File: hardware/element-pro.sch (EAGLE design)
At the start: 80 parts, among them J4 AMP FCI 10103594-0001LF, Q3 BSS138PW,115, Q4 BSS138PW,115, SW1 SPST_TACT-KMR2, U1 NEOPIXEL_NANO_2427, U10 TSL2591, U11 915MHz, U12 W25X40CLSNIG-ND-AT25F512BJEDE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, U14 SENSEAIR_S8, U15 VLP-450-F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

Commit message: v0.2 - design update
- moved T/RH sensor away from top
- moved thermistor + ADC away from top
- moved VOC sensor from bottom
- repositioned pressure sensor
- added more isolation to all necessary sensors
- a lot of trace and component placement adjustments
- added external voltage input
- ERC/DRC
- silkscreen update
- added gerbers
- NOTE: BOM not updated; untested design
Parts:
- added C14: 0.1uF, Adafruit Feather 32u4 Bluefruit LE:MICROBUILDER_CAP_CERAMIC_0402MP
- added J3: (no value), SparkFun-Connectors:CONN_022.54MM_SCREWTERM
- added R1, R2: 10K, Adafruit Feather 32u4 Bluefruit LE:MICROBUILDER_RESISTOR_0402MP
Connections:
- removed net AIN1: U4.AIN1
- new net AIN3: R1.2, U4.AIN3
- new net N$6: C14.2, J3.2, R1.1, R2.2
- net GND: now also C14.1, J3.1, R2.1
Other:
- note added: "0.2"
- note added: "External voltage input"
- note removed: "0.1"
- moved on the sheet: C13, C2, FB3, FB4, R12, U4

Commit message: branding modification
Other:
- note added: "0.3"
- note removed: "0.2"
- note removed: "ArchSense"
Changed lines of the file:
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@@
 <?xml version="1.0" encoding="utf-8"?>
 <!DOCTYPE eagle SYSTEM "eagle.dtd">
-<eagle version="9.4.1">
+<eagle version="9.1.1">
 <drawing>
 <settings>
@@
 <text x="-60.96" y="129.54" size="2.54" layer="94" font="vector">TagConnect ISP headers</text>
 <text x="241.3" y="-25.4" size="2.54" layer="94" font="vector">3.3V voltage regulator</text>
-<text x="248.412" y="-82.296" size="5.08" layer="94" font="vector" ratio="20">ArchSense</text>
-<text x="248.666" y="-74.422" size="2.54" layer="94" font="vector" ratio="10">Element Pro</text>
+<text x="245.872" y="-79.756" size="5.08" layer="94" font="vector" ratio="20">Element Pro</text>
 <text x="257.302" y="-112.522" size="2.54" layer="94" font="vector" ratio="10">Akram Ali</text>
 <text x="134.62" y="-30.48" size="2.54" layer="94" font="vector">USB + FTDI</text>
-<text x="257.556" y="-102.362" size="2.54" layer="94" font="vector" ratio="10">0.2</text>
-<text x="248.666" y="-87.122" size="2.54" layer="94" font="vector" ratio="10">github.com/akstudios</text>
+<text x="257.556" y="-102.362" size="2.54" layer="94" font="vector" ratio="10">0.3</text>
+<text x="246.126" y="-84.582" size="2.54" layer="94" font="vector" ratio="10">github.com/akstudios</text>
 <text x="160.02" y="101.6" size="1.778" layer="97" font="vector">0x29</text>
 <text x="208.28" y="76.2" size="2.54" layer="94" font="vector">RGB LED</text>

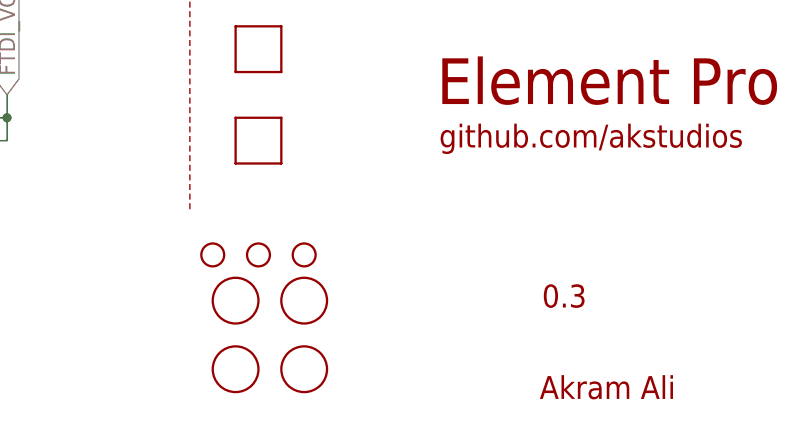
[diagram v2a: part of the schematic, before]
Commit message: v0.4 - repositioning sensors
- better heat management
- added more thermal breaks on board
- rearranged many traces
- erc/drc
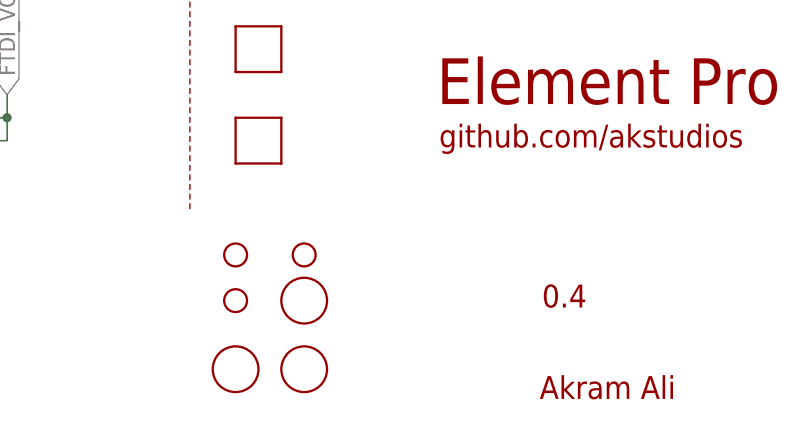
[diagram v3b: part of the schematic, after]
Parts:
- removed U$7: FIDUCIAL, adafruit:FIDUCIAL
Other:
- note added: "0.4"
- note removed: "0.3"
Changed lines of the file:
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@@
 <part name="SUPPLY21" library="SparkFun-Aesthetics" deviceset="VCC" device=""/>
 <part name="GND15" library="SparkFun-Aesthetics" deviceset="GND" device=""/>
-<part name="U$7" library="adafruit" deviceset="FIDUCIAL" device=""/>
 <part name="SW1" library="adafruit" deviceset="SPST_TACT" device="-KMR2"/>
 <part name="U14" library="SenseAir S8" deviceset="SENSEAIR_S8" device=""/>
@@
 <text x="257.302" y="-112.522" size="2.54" layer="94" font="vector" ratio="10">Akram Ali</text>
 <text x="134.62" y="-30.48" size="2.54" layer="94" font="vector">USB + FTDI</text>
-<text x="257.556" y="-102.362" size="2.54" layer="94" font="vector" ratio="10">0.3</text>
+<text x="257.556" y="-102.362" size="2.54" layer="94" font="vector" ratio="10">0.4</text>
 <text x="246.126" y="-84.582" size="2.54" layer="94" font="vector" ratio="10">github.com/akstudios</text>
 <text x="160.02" y="101.6" size="1.778" layer="97" font="vector">0x29</text>
@@
 <attribute name="VALUE" x="124.46" y="-99.06" size="1.778" layer="96"/>
 </instance>
-<instance part="H1" gate="G$1" x="220.98" y="-96.52" smashed="yes"/>
-<instance part="H2" gate="G$1" x="231.14" y="-96.52" smashed="yes"/>
+<instance part="H1" gate="G$1" x="223.52" y="-96.52" smashed="yes"/>
+<instance part="H2" gate="G$1" x="223.52" y="-101.6" smashed="yes"/>
 <instance part="FRAME1" gate="G$1" x="-71.12" y="-116.84" smashed="yes">
 <attribute name="DRAWING_NAME" x="248.031" y="-97.409" size="2.54" layer="94" font="vector"/>
@@
 <attribute name="VALUE" x="263.144" y="82.296" size="1.778" layer="96"/>
 </instance>
-<instance part="H3" gate="G$1" x="226.06" y="-96.52" smashed="yes"/>
+<instance part="H3" gate="G$1" x="231.14" y="-96.52" smashed="yes"/>
 <instance part="TC1" gate="A" x="-35.56" y="109.22" smashed="yes" rot="R180">
 <attribute name="VALUE" x="-31.75" y="116.84" size="1.778" layer="96" rot="R180"/>
@@
 <attribute name="VALUE" x="86.36" y="38.1" size="1.778" layer="96"/>
 </instance>
-<instance part="U$7" gate="G$1" x="223.52" y="-101.6" smashed="yes"/>
 <instance part="SW1" gate="G$1" x="86.36" y="48.26" smashed="yes">
 <attribute name="NAME" x="80.01" y="45.72" size="1.778" layer="95" rot="R90"/>
